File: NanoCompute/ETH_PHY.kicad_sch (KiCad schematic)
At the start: 52 parts, among them J1 2250506, U1 RTL8211F, U3 HSP051, U6 HSP051, Y1 25 MHz

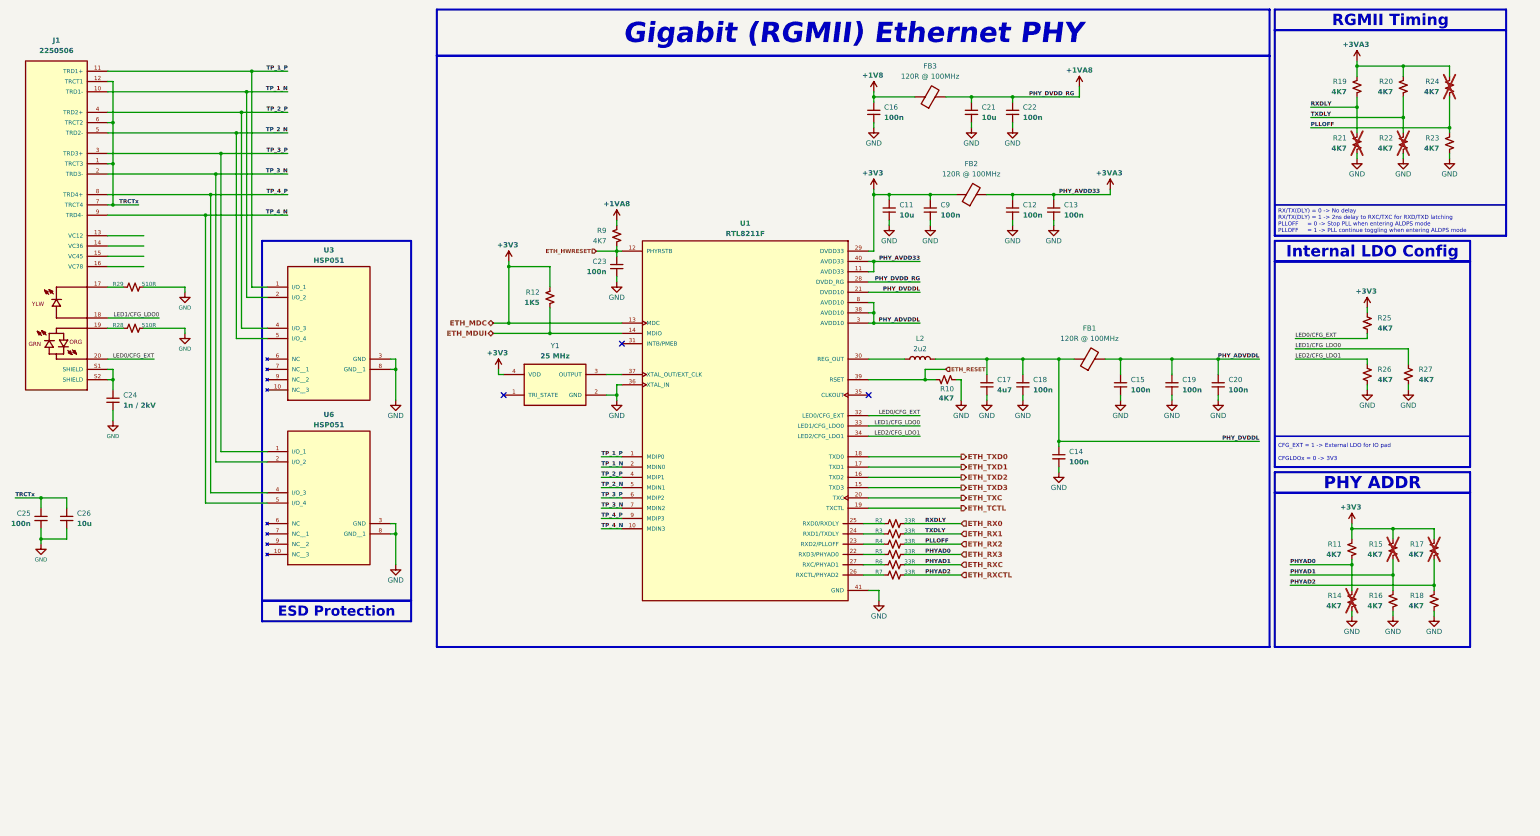
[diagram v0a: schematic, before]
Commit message: I think I added net classes(+coloring) for LPDDR4.
I'm not sure, it's 3AM I should check what I did tomorrow, figure our
those couple of signals that I don't understand where to connect or what
they are for. Probabbly could start working on the power section of the
LPDDR4. Need to check how much RAM will I actually need for 4K video
(@60fps?).
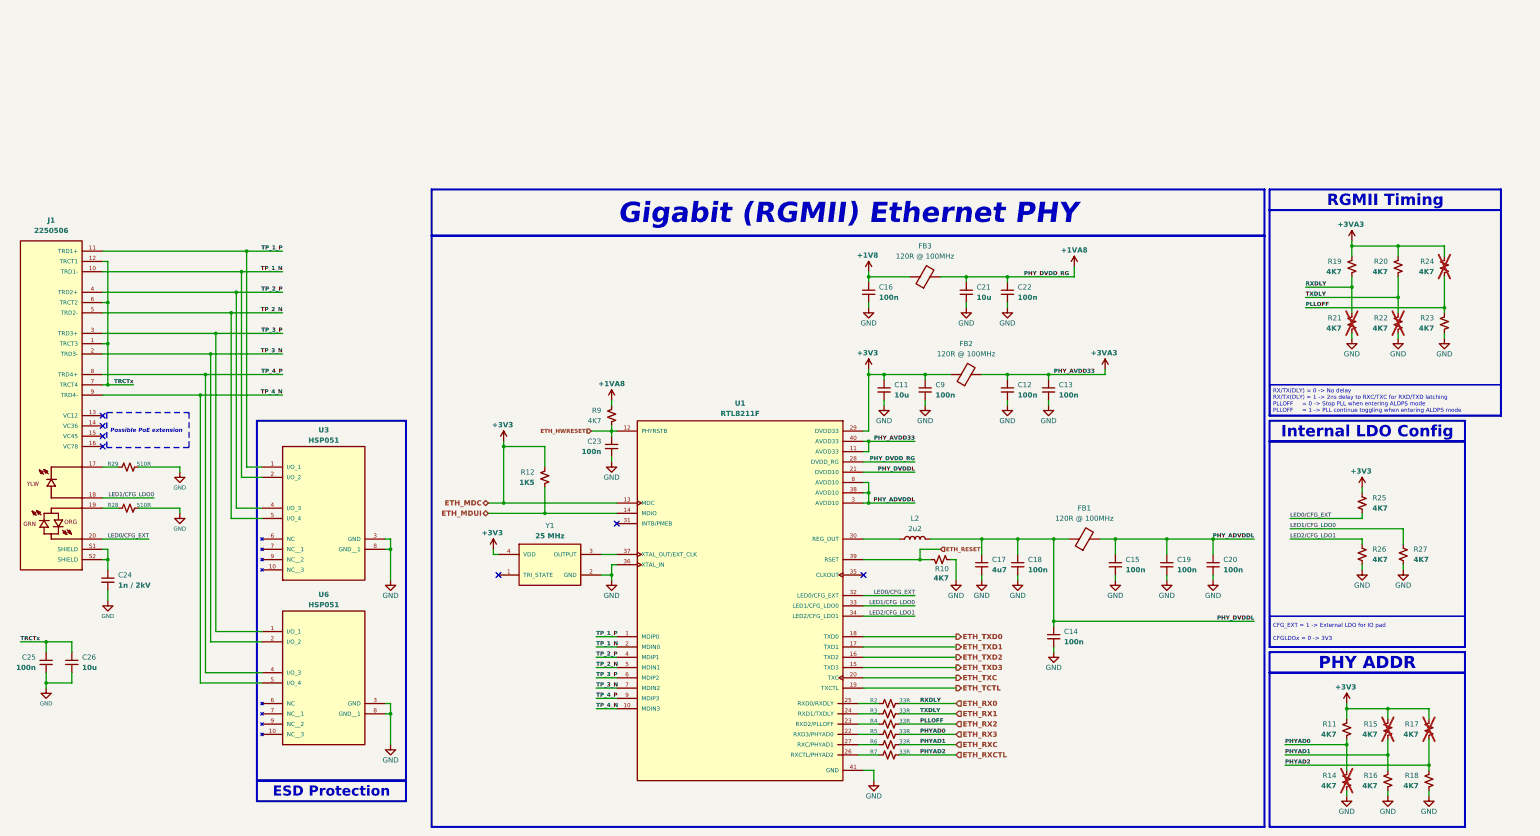
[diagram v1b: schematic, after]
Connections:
- no-connect marks 3 -> 7
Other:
- moved on the sheet: C11, C12, C13, C14, C15, C16, C17, C18, C19, C20, C21, C22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

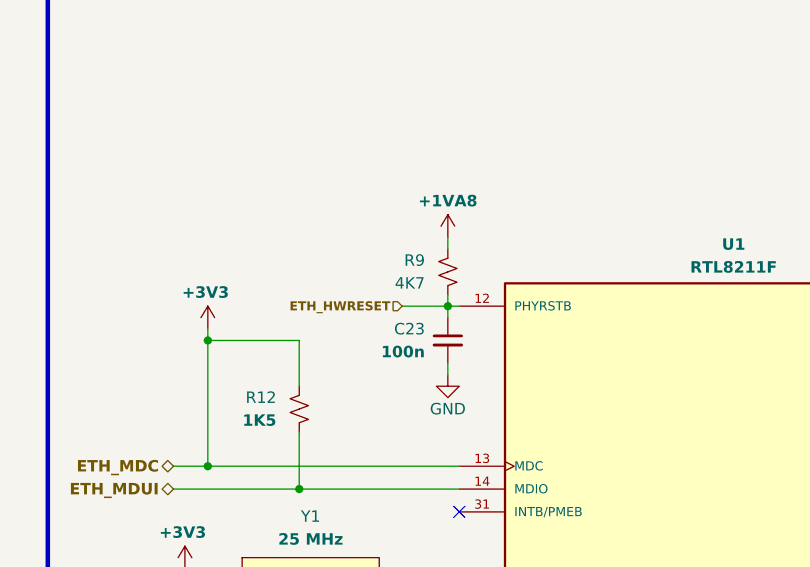
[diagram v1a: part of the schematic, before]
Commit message: Finished one LPDDR4 and connected it to LPDDR4 PHY
Connected the LPDDR4 to RK3588 LPDDR4 PHY, check all connections and it LGTM!
Added a second chip for additional 32Gb(4GB) LPDDR4 for total of 64Gb(8GB) of LPDRR4 memory.
Need to change nets for second chip from A->C and B->D.
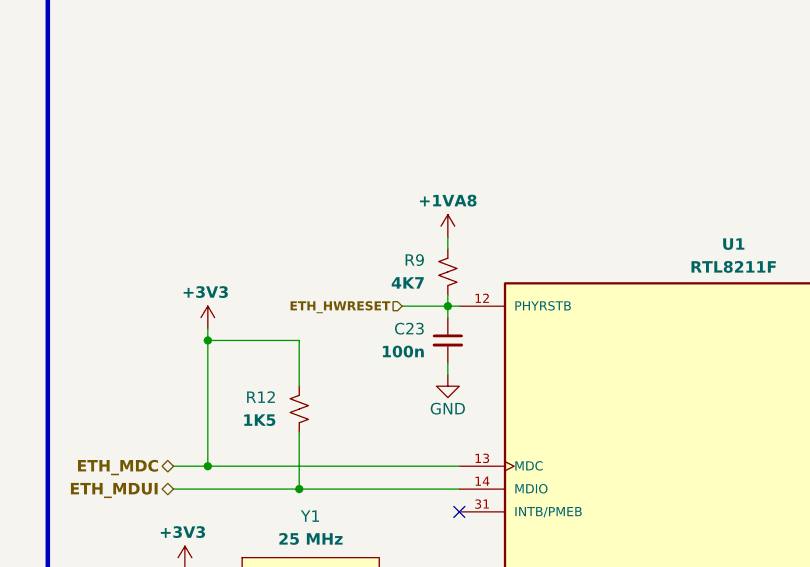
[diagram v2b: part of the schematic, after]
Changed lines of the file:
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@@
 				(font
 					(size 1.27 1.27)
+					(thickness 0.254)
+					(bold yes)
 				)
 				(justify left)

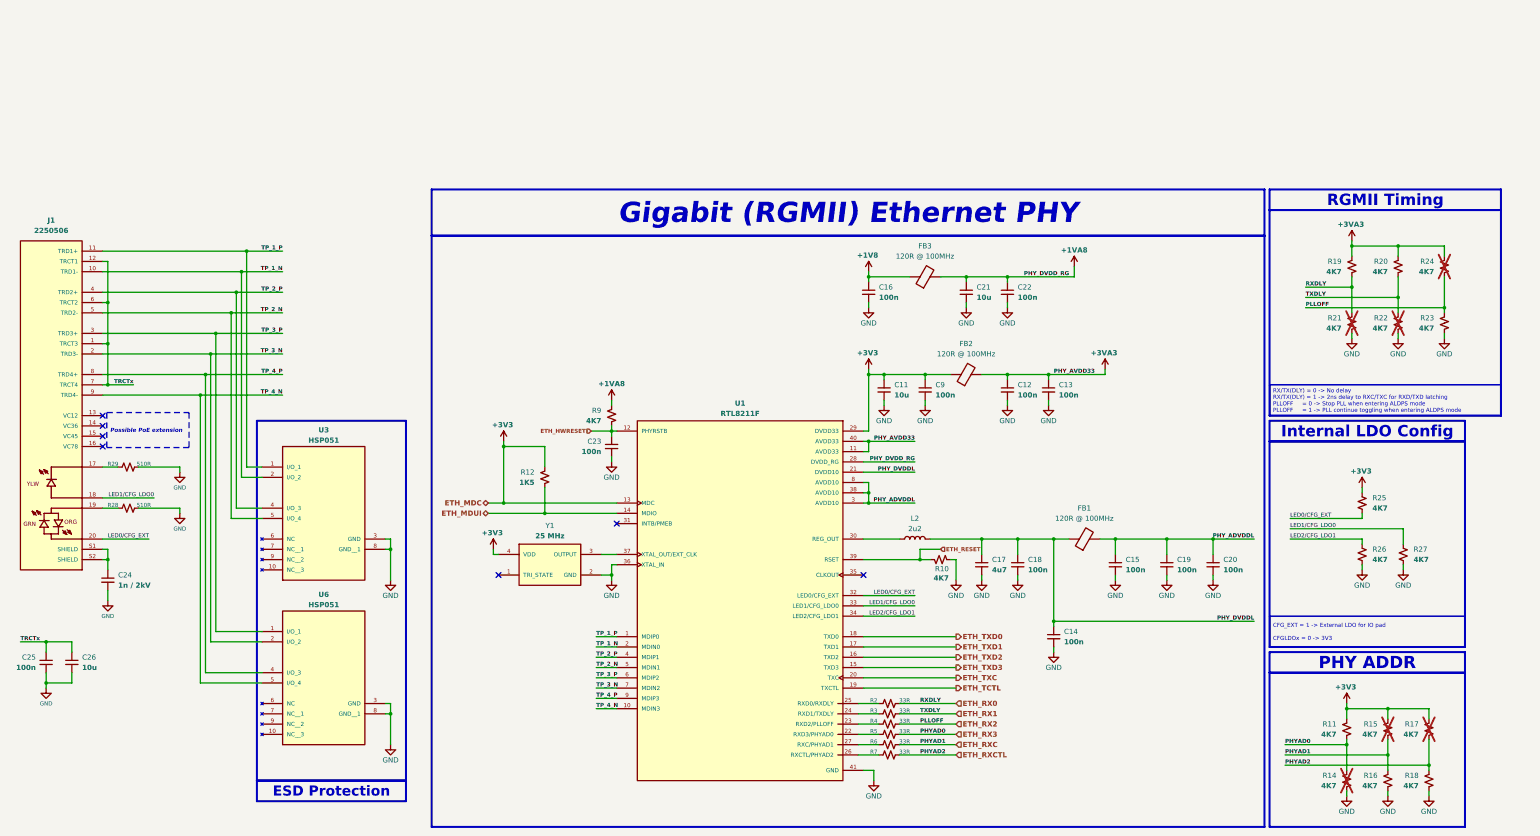
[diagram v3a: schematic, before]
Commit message: Added eMMC 5.1 HS400 128GB
It would act as a on-board primary storage while NVMe would act as an
extension/upgrade.
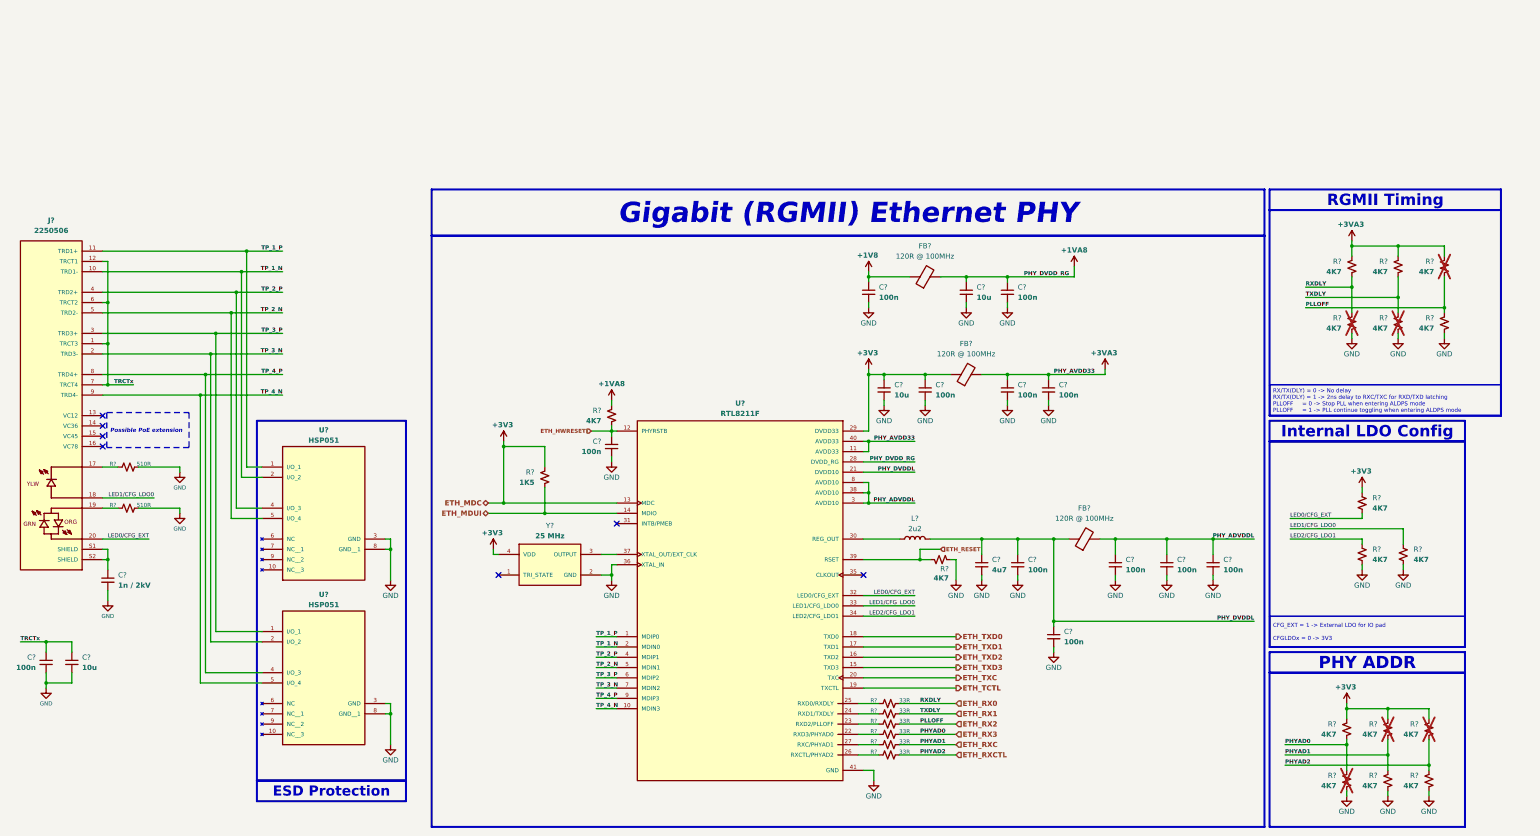
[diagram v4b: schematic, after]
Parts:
- renumbered C11 to C?, C20 to C?, C23 to C?, C13 to C?, C24 to C?, C21 to C?, C16 to C?, C18 to C?, C12 to C?, C15 to C?, C9 to C?, C14 to C?, C22 to C?, C25 to C?, C17 to C?, C26 to C?, C19 to C?, FB1 to FB?, FB3 to FB?, FB2 to FB?, J1 to J?, L2 to L?, R24 to R?, R25 to R?, R18 to R?, R15 to R?, R23 to R?, R27 to R?, R6 to R?, R12 to R?, R29 to R?, R4 to R?, R3 to R?, R9 to R?, R10 to R?, R21 to R?, R5 to R?, R2 to R?, R11 to R?, R19 to R?, R17 to R?, R22 to R?, R20 to R?, R14 to R?, R26 to R?, R28 to R?, R7 to R?, R16 to R?, U6 to U?, U3 to U?, U1 to U?, Y1 to Y?
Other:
- title: Curiosity Board -> NanoCompute
